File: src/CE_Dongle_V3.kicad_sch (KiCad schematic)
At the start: 13 parts, among them J10 Conn_01x02, J2 Conn_01x02, J3 Conn_01x02, J6 Conn_01x02, J7 8P8C_LED_Shielded, J8 Conn_01x02

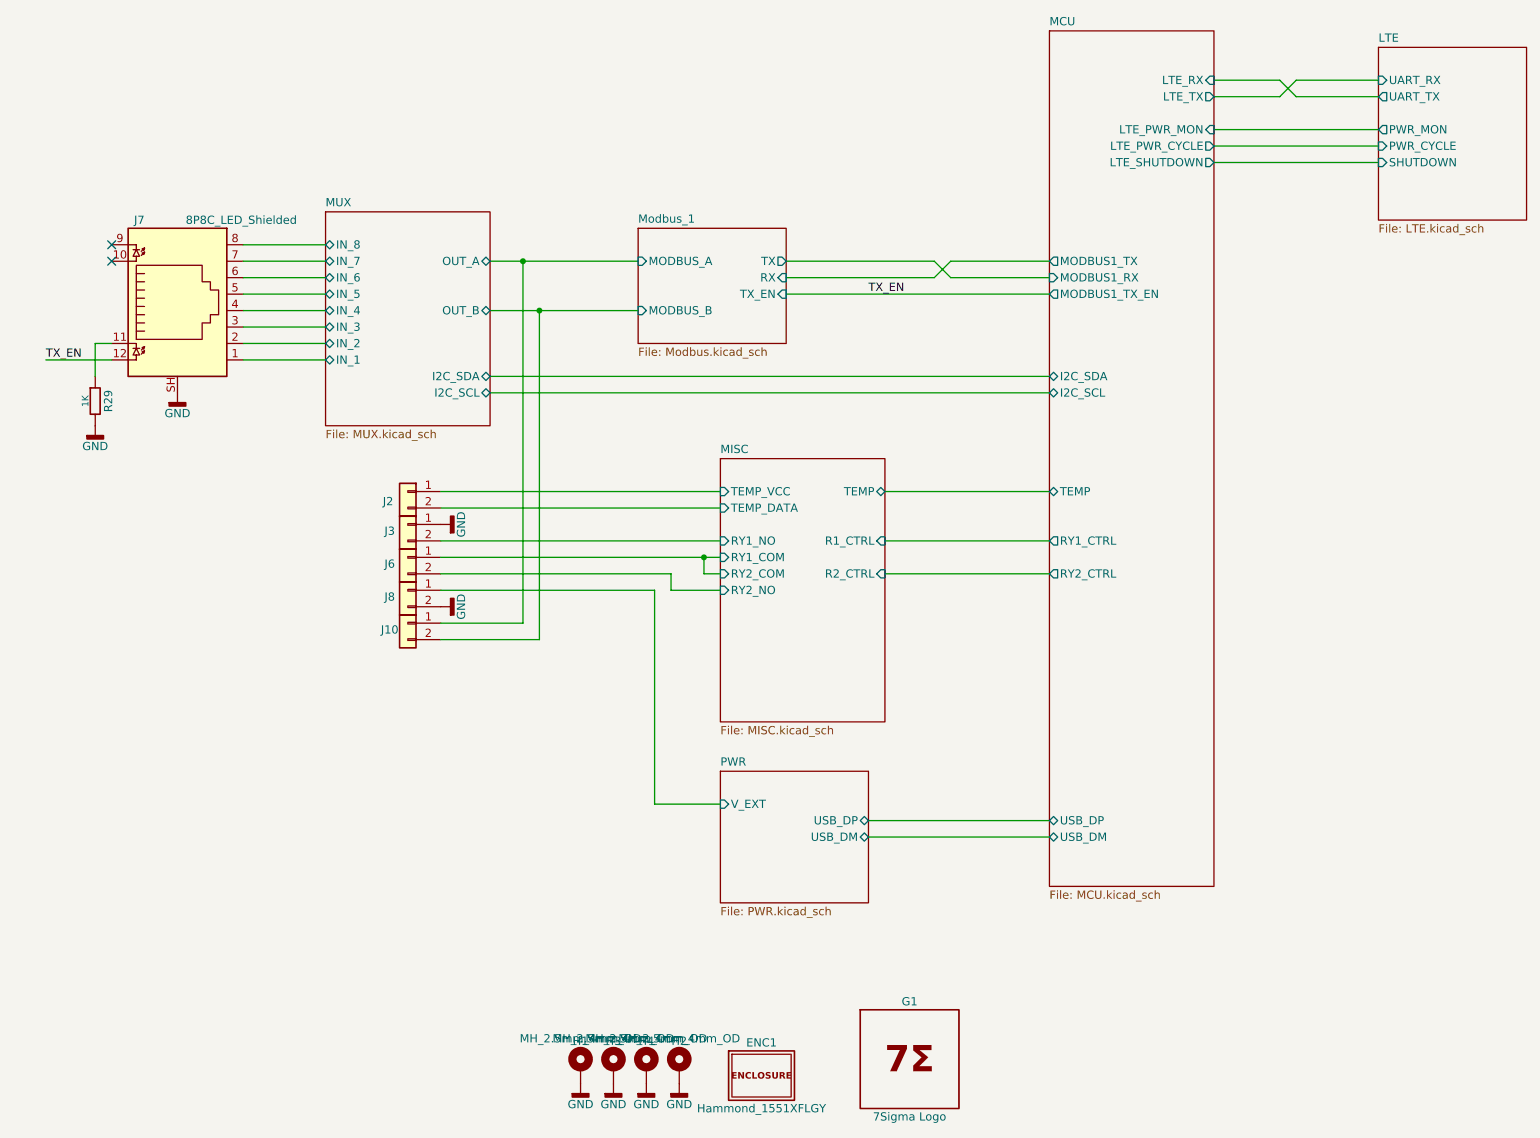
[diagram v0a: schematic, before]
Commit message: schematic cleanup, verification. GPIO9 pin pulldown changed to pullup.
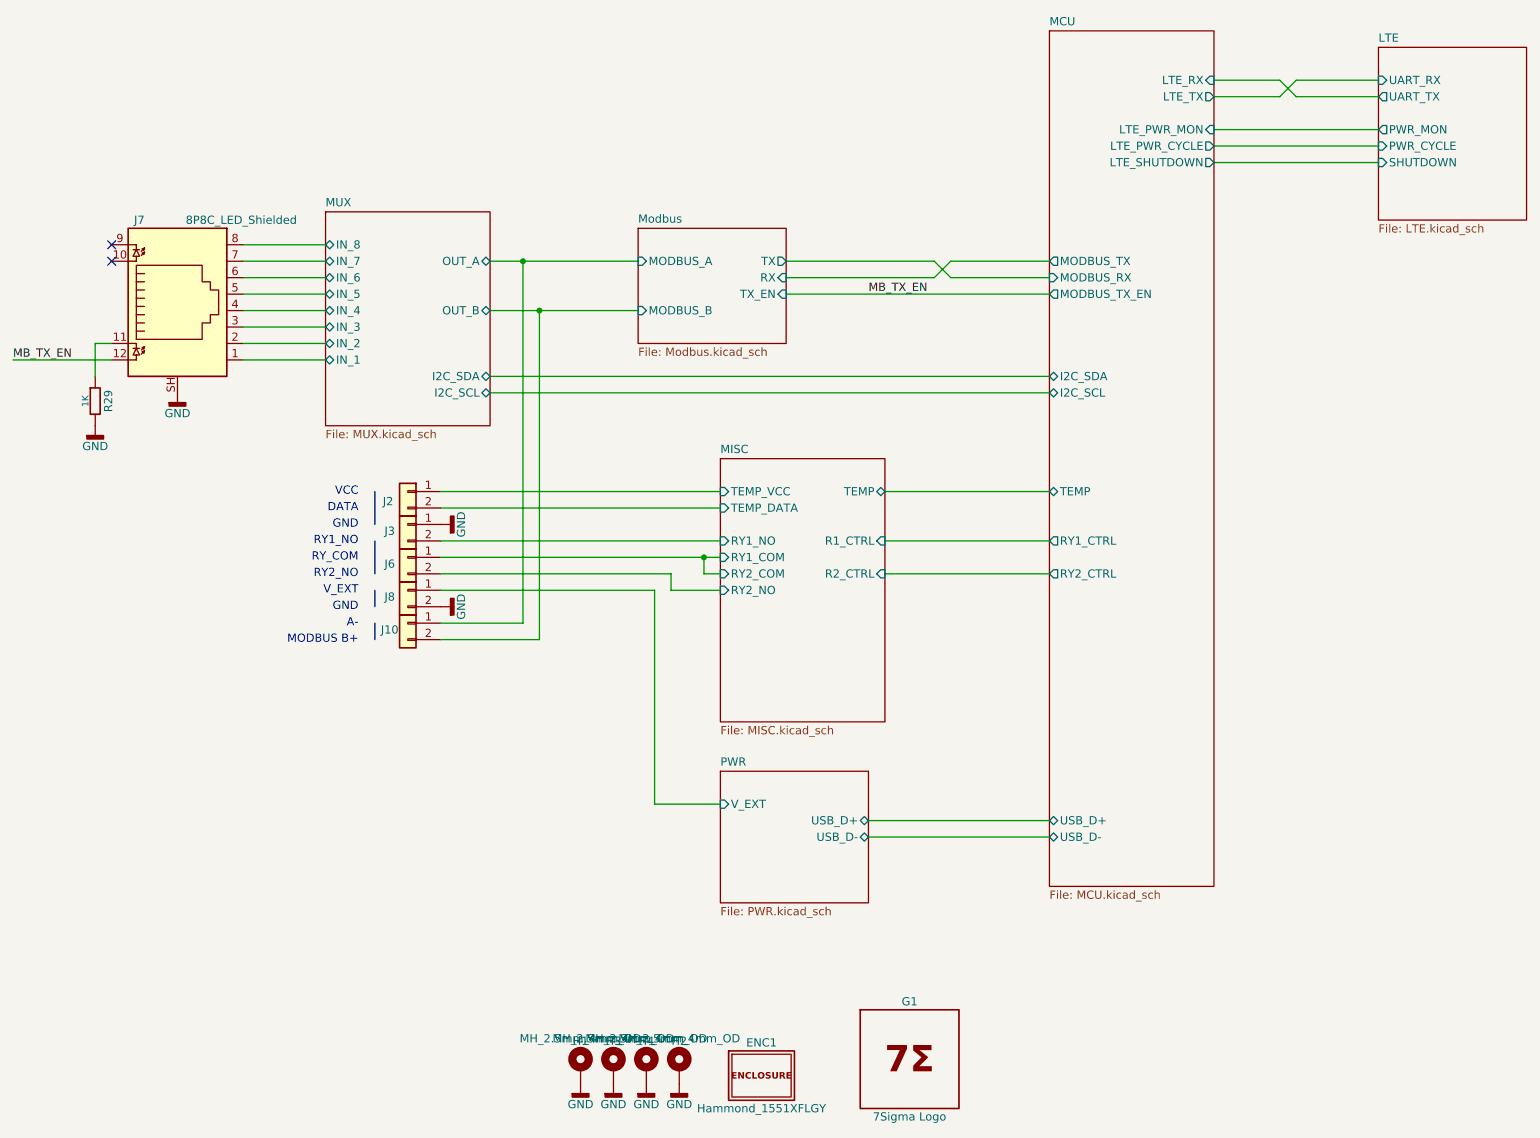
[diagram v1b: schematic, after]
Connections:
- net TX_EN renamed MB_TX_EN
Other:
- sheet Modbus_1 renamed Modbus
- sheet MCU ports: added MODBUS_RX, MODBUS_TX, MODBUS_TX_EN, USB_D+, USB_D-; removed MODBUS1_RX, MODBUS1_TX, MODBUS1_TX_EN, USB_DM, USB_DP
- sheet PWR ports: added USB_D+, USB_D-; removed USB_DM, USB_DP
- note added: "A-"
- note added: "DATA"
- note added: "GND"
- note added: "MODBUS B+"
- note added: "RY1_NO"
- note added: "RY2_NO"
- note added: "RY_COM"
- note added: "VCC"
- note added: "V_EXT"
